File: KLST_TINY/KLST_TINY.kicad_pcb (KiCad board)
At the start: 4 copper layers, 60 x 100 mm, 127 parts, among them J1 Micro_SD_Card_Card_Detect_SPI, J10 UART_00, J11 ADD-ON_PWR, J12 UART_01, J13 ADD-ON_AUDIO, J2 USB_A, J3 USB_B_Micro, J4 GPIO+ANALOG_IO_PINS, J5 ARM_JTAG_SWD(STDC14), J6 HEADPHONES+MIC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

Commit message: added note for ARM-JTAG connector
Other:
- board text added: "@TODO(maybe move ARM-JTAG connector away from USB connector ( for hand soldering or rotate by 90° … and make pads longer))"
- board text removed: "@TODO(maybe move ARM-JTAG connector away from USB connector( for hand soldering ))"

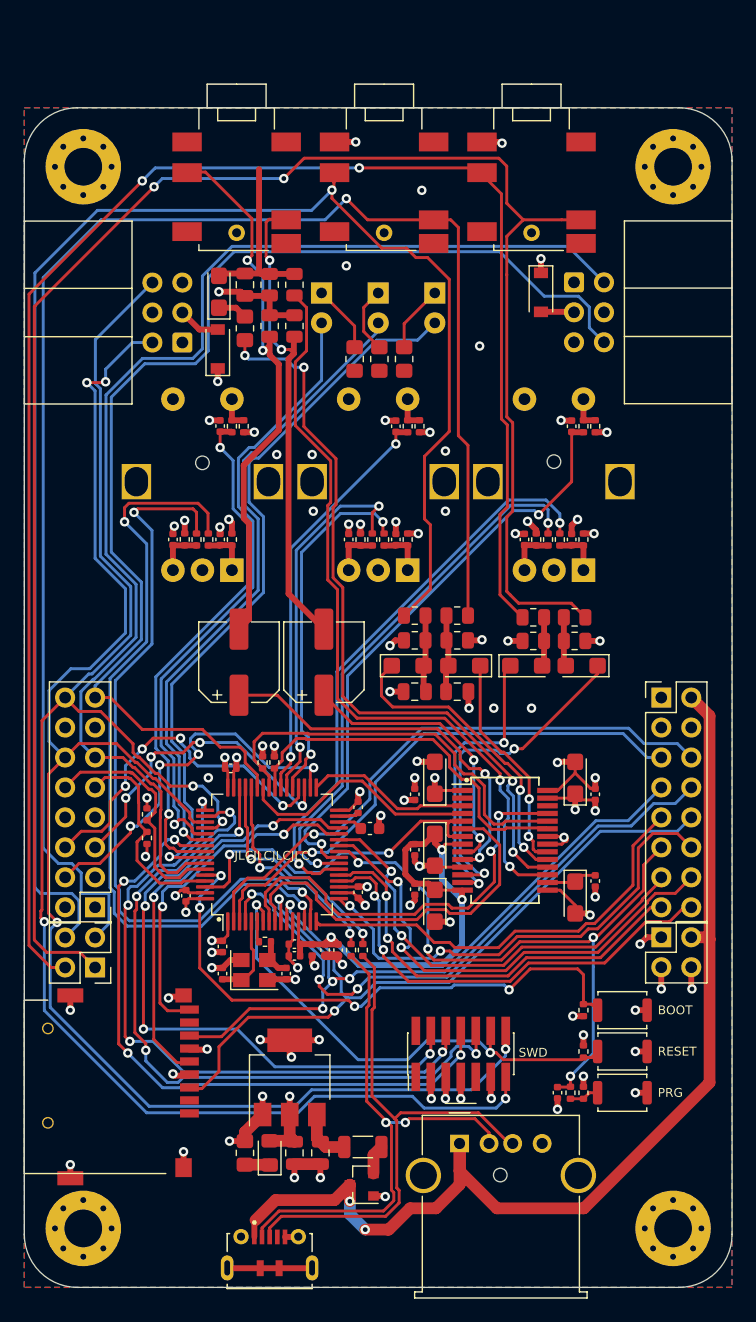
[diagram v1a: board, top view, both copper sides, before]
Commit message: fixed KLST_TINY reversed diode, minor changes to KLST_PANDA
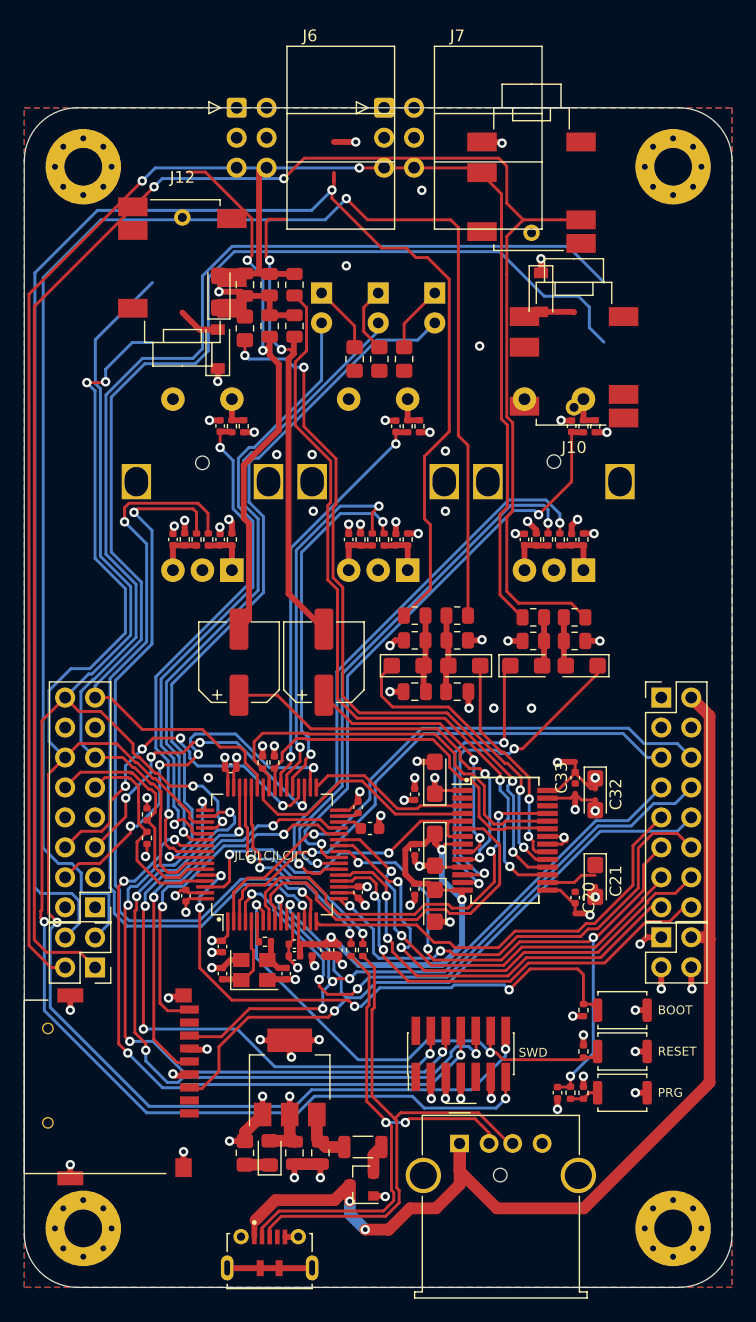
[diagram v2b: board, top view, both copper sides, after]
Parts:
- C20, C33: value 10uF -> 100nF; footprint Capacitor_Tantalum_SMD:CP_EIA-3216-18_Kemet-A -> Capacitor_SMD:C_0402_1005Metric
- C21, C32: value 100nF -> 10uF; footprint Capacitor_SMD:C_0402_1005Metric -> Capacitor_Tantalum_SMD:CP_EIA-3216-18_Kemet-A
- J10: value UART_00 -> LINE_IN; footprint Connector_IDC:IDC-Header_2x03_P2.54mm_Horizontal -> KLST_TINY:Korean_Hroparts_Elec_PJ-316A-6A
- J12: value UART_01 -> LINE_OUT; footprint Connector_IDC:IDC-Header_2x03_P2.54mm_Horizontal -> KLST_TINY:Korean_Hroparts_Elec_PJ-316A-6A
- J6: value HEADPHONES+MIC -> UART_00; footprint KLST_TINY:Korean_Hroparts_Elec_PJ-316A-6A -> Connector_IDC:IDC-Header_2x03_P2.54mm_Horizontal
- J7: value LINE_IN -> UART_01; footprint KLST_TINY:Korean_Hroparts_Elec_PJ-316A-6A -> Connector_IDC:IDC-Header_2x03_P2.54mm_Horizontal
- J8: value LINE_OUT -> HEADPHONES+MIC
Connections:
- C20 pad 1: Net-(C20-Pad1) -> GND
- C20 pad 2: GND -> +3.3VA
- C21 pad 1: Net-(C20-Pad1) -> +3.3VA
- C30 pad 2: +3.3VA -> +3V3
- C31 pad 1: +3.3VA -> +3V3
- C32 pad 1: GND -> Net-(U3-VMID)
- C32 pad 2: +3V3 -> GND
- C33 pad 1: +3V3 -> Net-(U3-VMID)
- D5 pad 1: +3V3 -> Net-(D5-K)
- D5 pad 2: Net-(D5-Pad2) -> +3V3
- D6 pad 1: +3V3 -> Net-(D6-K)
- D6 pad 2: Net-(D6-Pad2) -> +3V3
- J1 pad 1: (no net) -> unconnected-(J1-NC-Pad1)
- J1 pad 2: /GPIO_09 -> /GPIO_07
- J1 pad 3: /GPIO_04 -> /SDCARD_MOSI
- J1 pad 5: /GPIO_09 -> /SDCARD_SCK
- J1 pad 7: /GPIO_03 -> /SDCARD_MISO
- J1 pad 8: (no net) -> unconnected-(J1-NC-Pad8)
- J1 pad 9: /GPIO_08 -> /GPIO_06
- J3 pad 4: (no net) -> unconnected-(J3-ID-Pad4)
- J5 pad 1: (no net) -> unconnected-(J5-NC-Pad1)
- J5 pad 10: /SWD_SWI -> /SPI_00_CS
- J5 pad 2: (no net) -> unconnected-(J5-NC-Pad2)
- J5 pad 8: /SWD_SWO -> /SPI_00_SCK
- J5 pad 9: (no net) -> unconnected-(J5-JRCLK/NC-Pad9)
- J8 pad R1: /LINE_OUT_RIGHT -> /audio_codec_WM8731/HEADPHONE_RIGHT
- J8 pad R1N: (no net) -> unconnected-(J8-PadR1N)
- J8 pad R2: (no net) -> GND
- J8 pad S: GND -> /audio_codec_WM8731/MIC_IN
- J8 pad T: /LINE_OUT_LEFT -> /audio_codec_WM8731/HEADPHONE_LEFT
- J8 pad TN: (no net) -> unconnected-(J8-PadTN)
- J9 pad 3: GND -> /SPI_00_CS
- U1 pad 10: /GPIO_03 -> /GPIO_02
- U1 pad 11: /GPIO_04 -> /GPIO_03
- U1 pad 16: /GPIO_05 -> /GPIO_04
- U1 pad 17: /GPIO_06 -> /GPIO_05
- U1 pad 2: /GPIO_00 -> /LED_00
- U1 pad 25: /GPIO_07 -> /GPIO_06
- U1 pad 28: /GPIO_08 -> /GPIO_07
- U1 pad 29: /GPIO_09 -> /ENCODER_02_BUTTON
- U1 pad 3: /GPIO_01 -> /GPIO_00
- U1 pad 34: /SPI_00_SCK -> /SDCARD_SCK
- U1 pad 35: /SPI_00_MISO -> /SDCARD_MISO
- U1 pad 36: /SPI_00_MOSI -> /SDCARD_MOSI
- U1 pad 4: /GPIO_02 -> /GPIO_01
- U1 pad 50: /SWD_SWI -> /SPI_00_CS
- U1 pad 55: /SWD_SWO -> /SPI_00_SCK
- U1 pad 56: /ENCODER_02_BUTTON -> /SPI_00_MISO
- U1 pad 57: /LED_00 -> /SPI_00_MOSI
- U3 pad 16: Net-(C20-Pad1) -> Net-(U3-VMID)
- U3 pad 2: (no net) -> unconnected-(U3-CLKOUT-Pad2)
- U3 pad 26: (no net) -> unconnected-(U3-XTO-Pad26)
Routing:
- net /SWD_SWI: track 61.2 -> 0.00 mm, vias 4 -> 0
- net /SPI_00_CS: track 0.00 -> 61.2 mm, vias 0 -> 4
- net /SWD_SWO: track 56.7 -> 0.00 mm, vias 4 -> 0
- net /SPI_00_SCK: track 33.1 -> 89.7 mm, vias 4 -> 8
- net /ENCODER_02_BUTTON: track 44.4 -> 78.7 mm, vias 2 -> 4
- net /GPIO_09: track 34.4 -> 0.00 mm, vias 2 -> 0
- net (no net): track 0.00 -> 32.7 mm
- net /GPIO_08: track 29.9 -> 0.00 mm, vias 2 -> 0
- net Net-(U3-VMID): track 0.00 -> 4.30 mm
- net Net-(C20-Pad1): track 4.30 -> 0.00 mm
- net Net-(D6-Pad2): track 3.60 -> 0.00 mm
- net Net-(D5-Pad2): track 2.82 -> 0.00 mm
- net /audio_codec_WM8731/MIC_IN: track 16.1 -> 18.0 mm, vias 0 -> 1
- net GND: track 119.3 -> 117.4 mm, vias 67 -> 66
- net +3V3: track 61.5 -> 62.8 mm, vias 35 -> 33
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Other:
- net class Default removed
- net class Power removed
- net class Power+ removed
